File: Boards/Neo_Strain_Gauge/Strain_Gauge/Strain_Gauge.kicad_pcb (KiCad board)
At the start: 2 copper layers, 85 x 56 mm, 59 parts, among them J1 Screw_Terminal_01x03, J2 Screw_Terminal_01x03, J3 Screw_Terminal_01x03, J4 Screw_Terminal_01x03, J5 Conn_01x02, J6 USB_B_Micro, J7 Conn_02x10_Counter_Clockwise, J8 Conn_02x12_Counter_Clockwise, U1 W25Q128JVS, U2 NCP1117-3.3_SOT223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

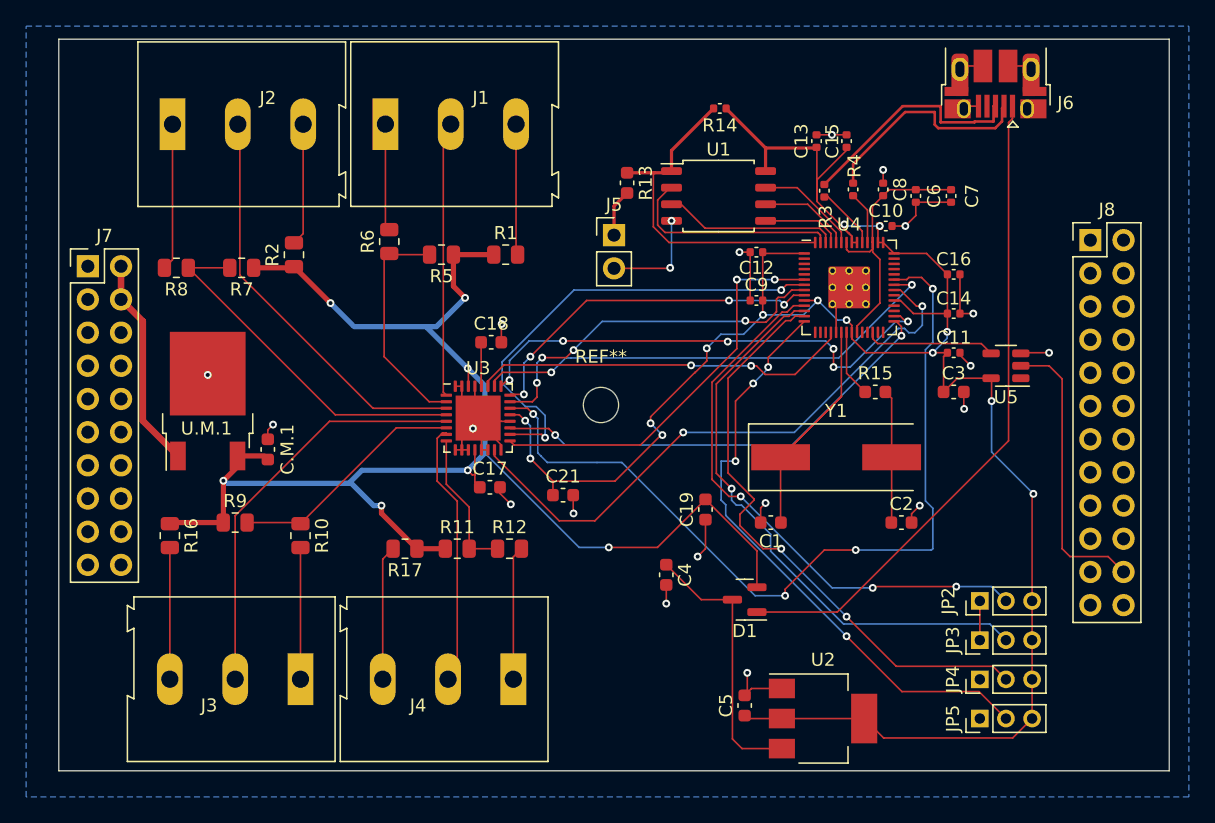
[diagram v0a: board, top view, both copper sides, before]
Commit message: Update to latest schematic and board design slots.
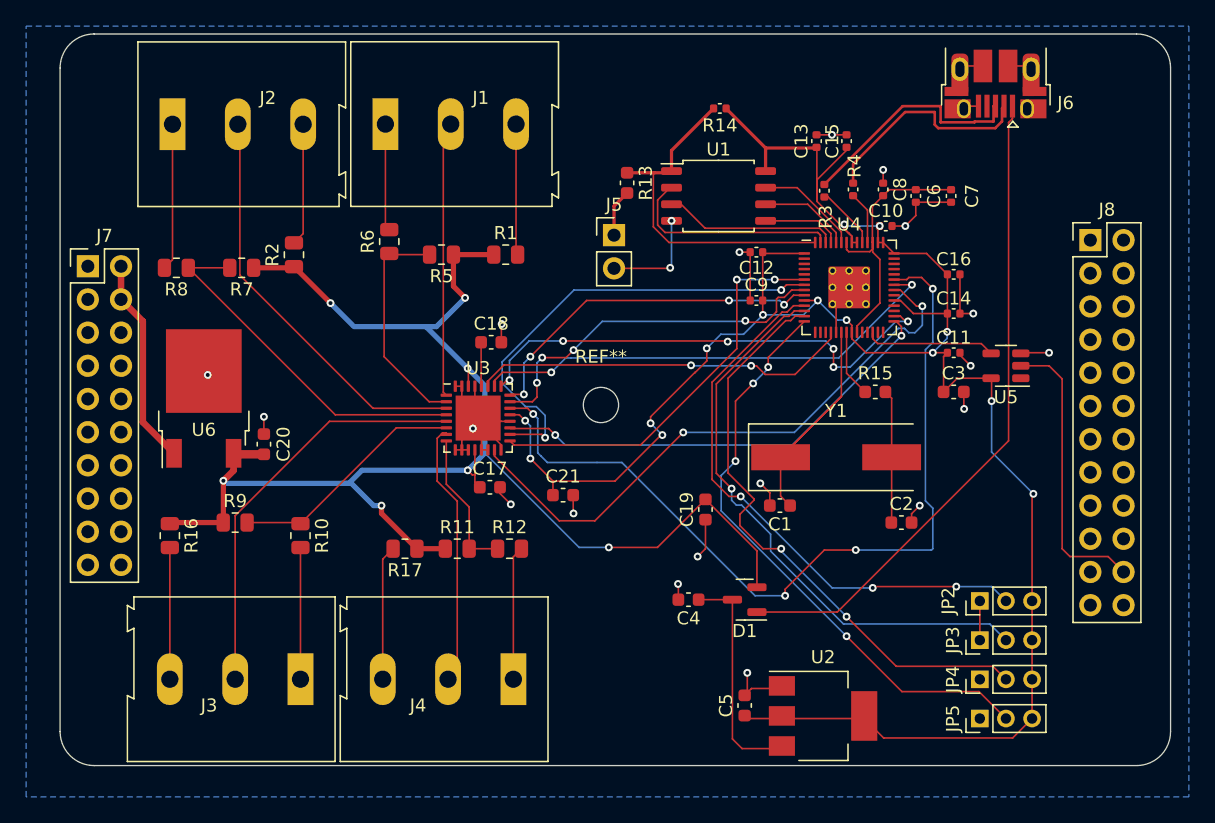
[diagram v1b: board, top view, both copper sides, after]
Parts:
- removed C.M.1: 10u, Capacitor_SMD:C_0603_1608Metric
- removed U.M.1: KA78M05_TO252, Package_TO_SOT_SMD:TO-252-2
- added C20: 10u, Capacitor_SMD:C_0603_1608Metric, F.Cu at (116.2, 85.0)
- added U6: KA78M05_TO252, Package_TO_SOT_SMD:TO-252-2, F.Cu at (111.6, 81.5)
- C21: value 0.1uF -> 100n
- moved C4 2.55 mm to (148.7, 96.9), turned to 180 degrees
- moved C1 1.48 mm to (155.7, 89.7)
- moved U2 0.20 mm to (159.0, 105.8)
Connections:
- J1 pad 1: Net-(J1-Pad1) -> GND
- J2 pad 1: Net-(J2-Pad1) -> GND
- J3 pad 1: Net-(J3-Pad1) -> GND
- J4 pad 1: Net-(J4-Pad1) -> GND
- R10 pad 2: Net-(J3-Pad1) -> GND
- R12 pad 2: Net-(J4-Pad1) -> GND
- R6 pad 2: Net-(J1-Pad1) -> GND
- R8 pad 2: Net-(J2-Pad1) -> GND
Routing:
- net GND: track 79.1 -> 119.0 mm
- net Net-(J2-Pad1): track 11.2 -> 0.00 mm
- net Net-(J4-Pad1): track 10.2 -> 0.00 mm
- net Net-(J3-Pad1): track 10.1 -> 0.00 mm
- net Net-(J1-Pad1): track 8.20 -> 0.00 mm
- net Net-(C4-Pad1): track 20.9 -> 17.3 mm
- net +5V: track 115.7 -> 117.8 mm
- net /XIN: track 23.1 -> 22.1 mm
- net /GPIO11: track 46.2 -> 45.5 mm
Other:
- outline, holes or cut-outs redrawn
- board text added: "SDAQ Strain Gauge Board Revision A Hugh Gallo 917-485-1788 RIOT Racing/RIT Baja"

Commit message: More strain gauge work to get in-stock parts
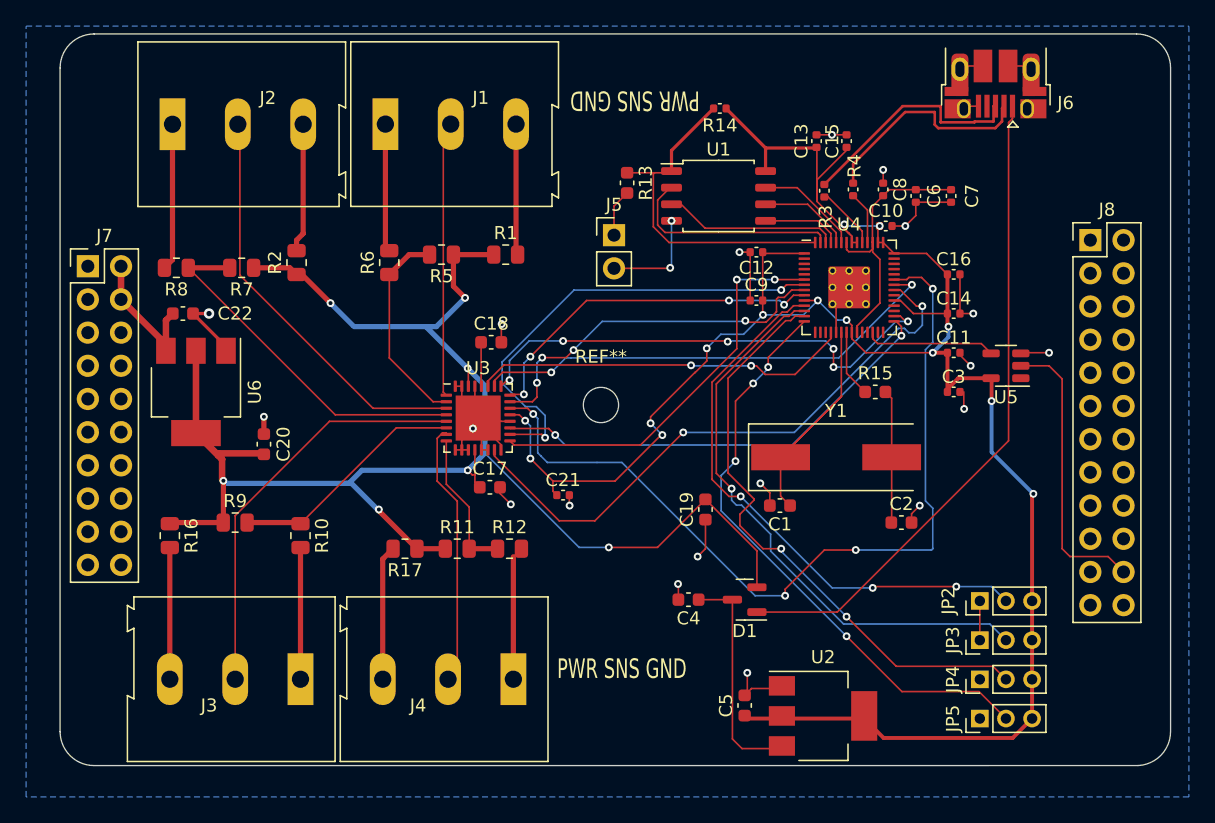
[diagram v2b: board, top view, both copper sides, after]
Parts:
- added C22: 10u, Capacitor_SMD:C_0603_1608Metric, F.Cu at (110.0, 75.0)
- C20: value 10u -> 22u
- C21, C3: footprint Capacitor_SMD:C_0603_1608Metric -> Capacitor_SMD:C_0402_1005Metric
- U6: value KA78M05_TO252 -> AZ1117-5.0; footprint Package_TO_SOT_SMD:TO-252-2 -> Package_TO_SOT_SMD:SOT-223-3_TabPin2
- moved R6 1.61 mm to (125.8, 71.1)
- moved U6 0.78 mm to (111.0, 81.0), turned to -90 degrees
- moved R2 0.63 mm to (118.7, 71.1)
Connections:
- net Net-(C4-Pad1) renamed /REG_POWER
- net Net-(D1-Pad1) renamed /VBUS
- U6 pad 1: /rpi_5v -> GND
- U6 pad 2: GND -> +5V
- U6 pad 3: +5V -> /rpi_5v
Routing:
- net +5V: track 117.8 -> 127.9 mm
- net GND: track 119.0 -> 125.0 mm
- net /rpi_5v: track 16.0 -> 11.0 mm
- net Net-(R5-Pad2): track 17.4 -> 15.9 mm
- net Net-(J2-Pad3): track 9.37 -> 9.89 mm
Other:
- board text added: "PWR SNS GND"

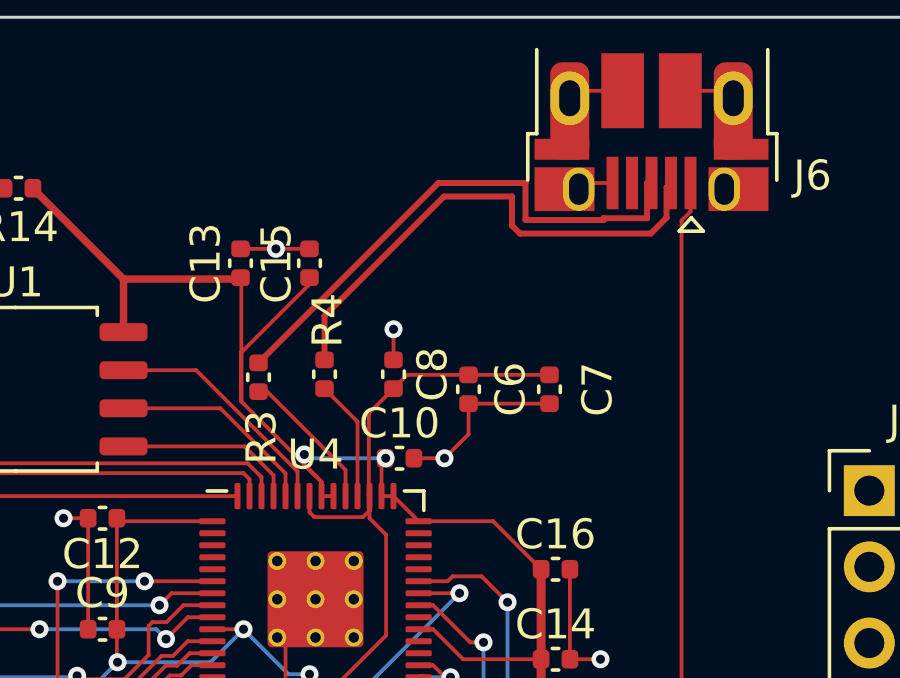
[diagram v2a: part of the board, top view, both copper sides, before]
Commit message: Make the USB differential pairing better
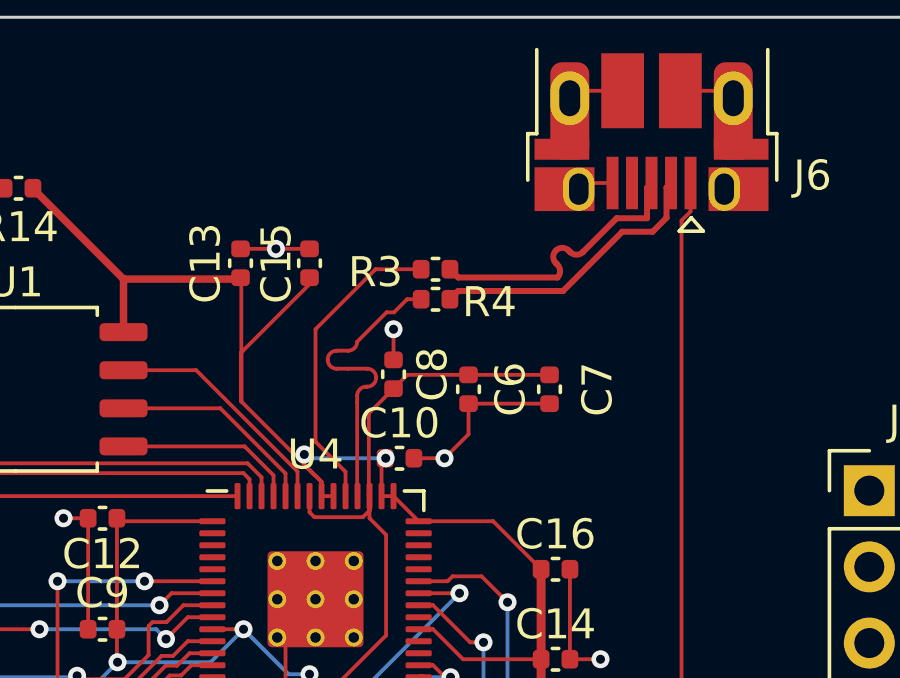
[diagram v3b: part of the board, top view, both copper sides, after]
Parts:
- moved R3 6.91 mm to (165.0, 62.0), turned to 180 degrees
- moved R4 4.47 mm to (165.0, 63.0), turned to 180 degrees
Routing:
- net /USB_D+: track 18.1 -> 9.52 mm
- net /USB_D-: track 17.0 -> 9.57 mm
- net /USB_DR-: track 4.04 -> 10.3 mm
- net /USB_DR+: track 4.85 -> 10.3 mm

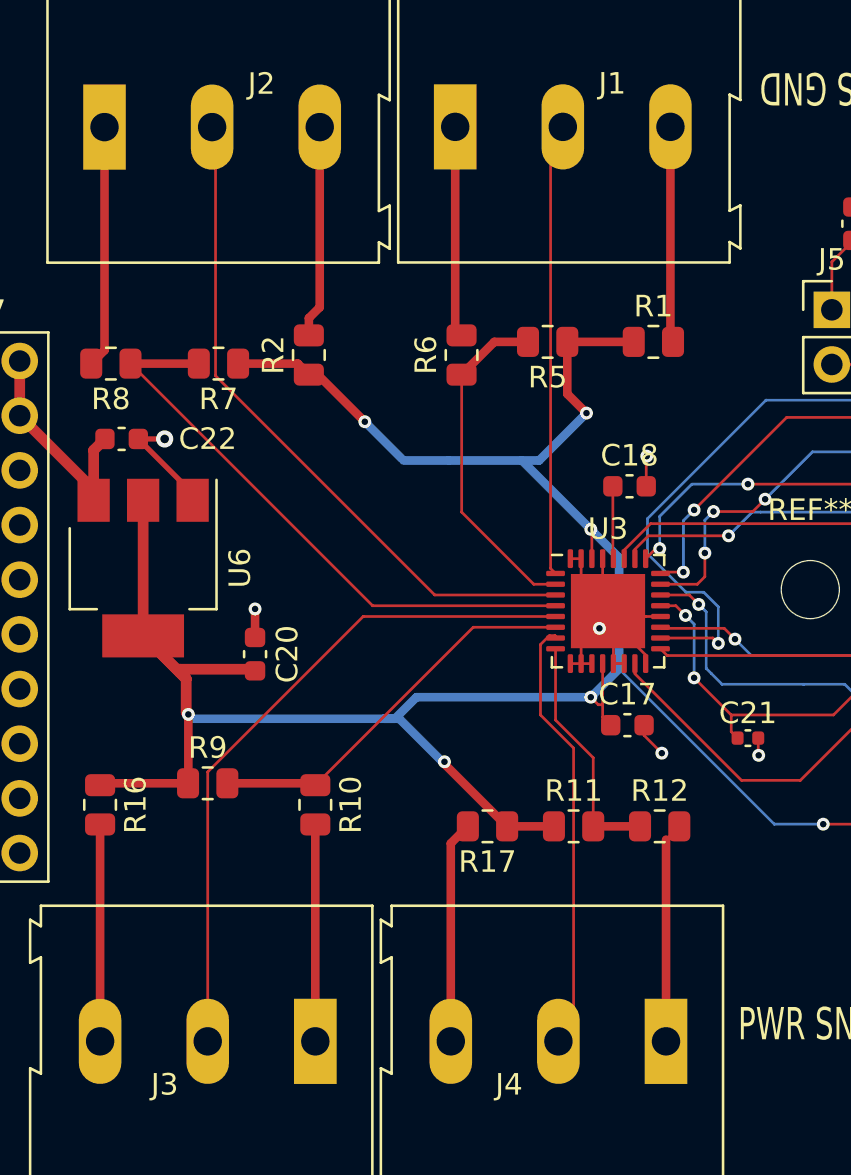
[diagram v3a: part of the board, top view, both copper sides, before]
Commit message: Improve differential pairing.
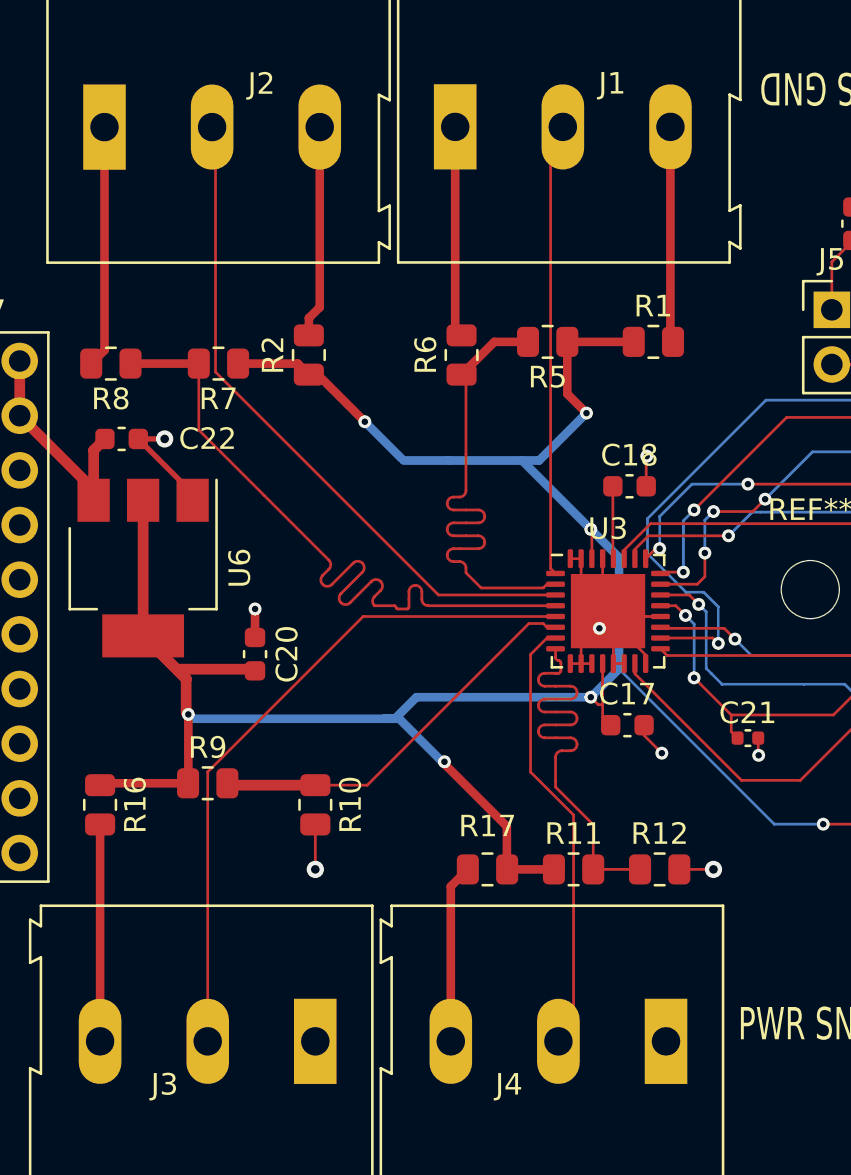
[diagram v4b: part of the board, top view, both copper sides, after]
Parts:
- moved R11 2.00 mm to (131.0, 95.0)
- moved R12 2.00 mm to (135.0, 95.0)
- moved R17 2.00 mm to (127.0, 95.0)
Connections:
- net Net-(J1-Pad2) renamed /IN3-
- net Net-(J2-Pad2) renamed /IN2-
- net Net-(J3-Pad2) renamed /IN1-
- net Net-(J4-Pad2) renamed /IN0-
- net Net-(R10-Pad1) renamed /IN1+
- net Net-(R11-Pad2) renamed /IN0+
- net Net-(R5-Pad2) renamed /IN3+
- net Net-(R7-Pad2) renamed /IN2+
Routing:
- net GND: track 125.0 -> 108.4 mm, vias 21 -> 23
- net /IN0+: track 11.1 -> 22.4 mm
- net /IN3+: track 15.9 -> 24.6 mm
- net /IN2+: track 27.6 -> 34.5 mm
- net Net-(J4-Pad3): track 10.3 -> 8.32 mm
- net +5V: track 127.9 -> 129.9 mm

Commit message: Even more minor updates to the boards
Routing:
- net /IN1+: track 18.5 -> 35.5 mm
- net /VBUS: track 50.4 -> 55.2 mm
- net GND: track 108.4 -> 106.9 mm, vias 23 -> 24
- net /GPIO25: track 65.4 -> 64.1 mm
- net /GPIO6: track 28.3 -> 28.1 mm, vias 4 -> 2

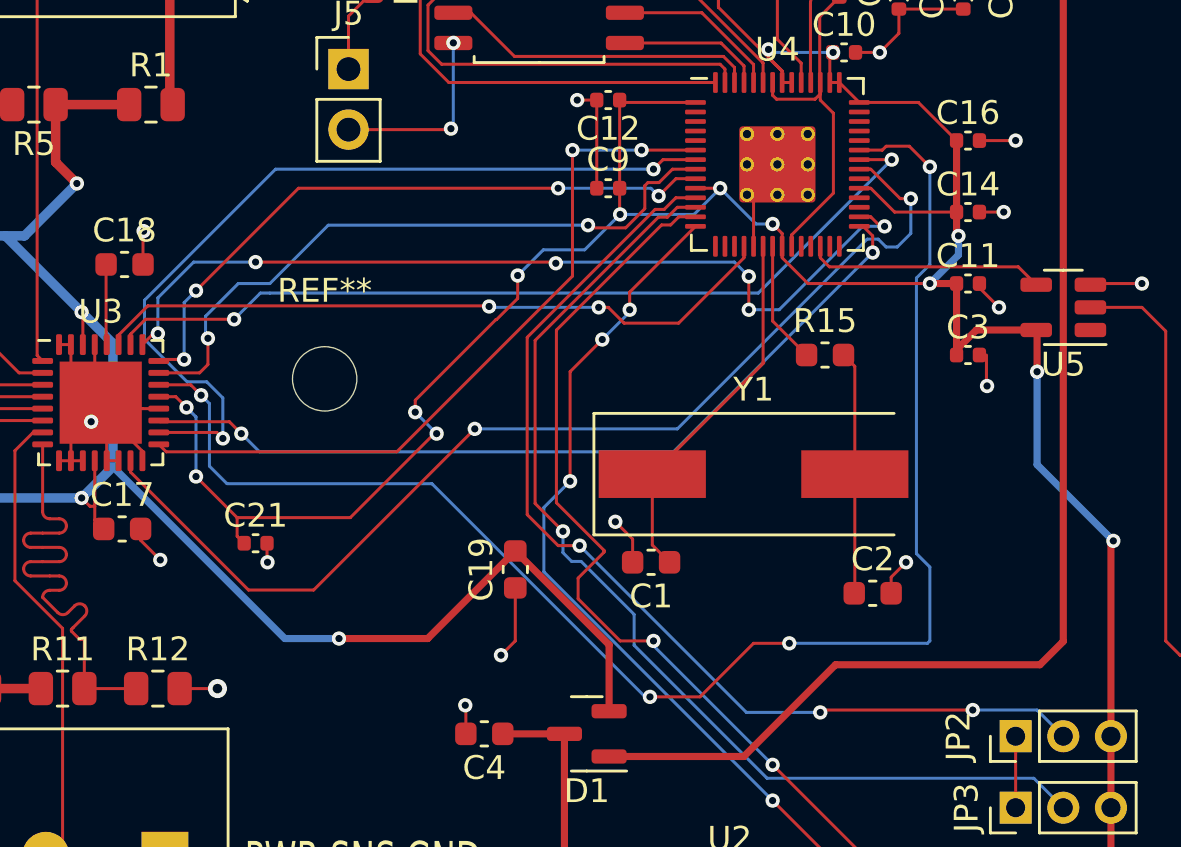
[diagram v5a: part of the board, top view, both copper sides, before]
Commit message: It's apparently possible to communicate over SPI to the ADC
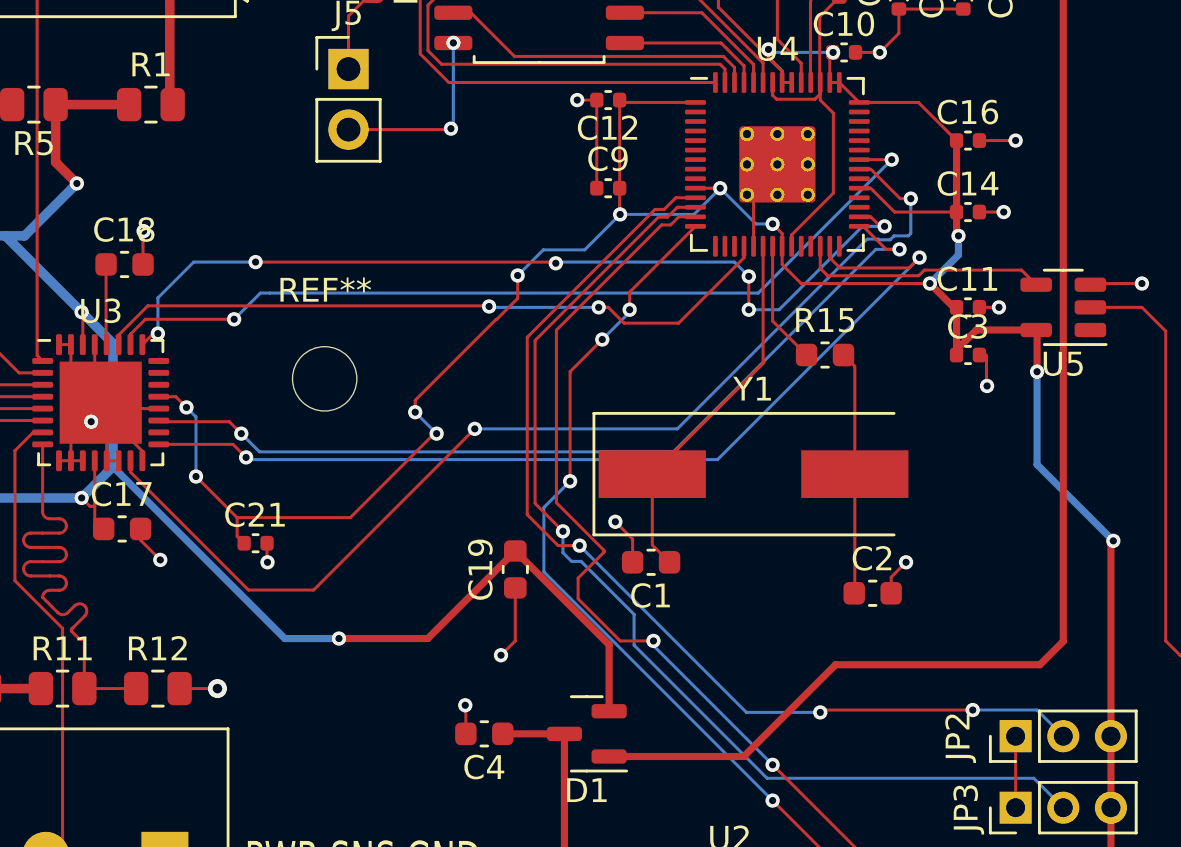
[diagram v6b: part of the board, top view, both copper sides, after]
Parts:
- moved C11 1.00 mm to (169.0, 79.0)
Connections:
- U3 pad 17: /GPIO4 -> /GPIO16
- U3 pad 18: /GPIO5 -> unconnected-(U3-Pad18)
- U3 pad 22: /GPIO25 -> unconnected-(U3-Pad22)
- U3 pad 23: /GPIO6 -> unconnected-(U3-Pad23)
- U3 pad 24: /GPIO7 -> unconnected-(U3-Pad24)
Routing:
- net /GPIO25: track 64.1 -> 0.00 mm, vias 4 -> 0
- net /GPIO16: track 0.00 -> 40.3 mm, vias 0 -> 2
- net /GPIO5: track 36.0 -> 0.00 mm, vias 2 -> 0
- net /GPIO4: track 31.0 -> 0.00 mm, vias 2 -> 0
- net /GPIO6: track 28.1 -> 0.00 mm, vias 2 -> 0
- net /GPIO7: track 27.4 -> 0.00 mm, vias 4 -> 0
- net /GPIO18: track 35.4 -> 37.3 mm
- net GND: track 106.9 -> 106.4 mm
